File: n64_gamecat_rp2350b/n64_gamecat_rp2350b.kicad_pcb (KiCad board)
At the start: 2 copper layers, 66 x 98 mm, 3 parts, among them U4 RP235x-B

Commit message: V0.6 PCB
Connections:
- U4 pad 1: unconnected-(U4-GPIO0-Pad1) -> CO_AD4
- U4 pad 10: unconnected-(U4-GPIO9-Pad10) -> CO_AD15
- U4 pad 2: unconnected-(U4-GPIO1-Pad2) -> CO_AD11
- U4 pad 3: unconnected-(U4-GPIO2-Pad3) -> CO_AD3
- U4 pad 31: unconnected-(U4-GPIO30-Pad31) -> CO_AD7
- U4 pad 32: READ -> CO_AD8
- U4 pad 33: WRITE -> CO_AD6
- U4 pad 34: ALE_L -> CO_AD9
- U4 pad 35: ALE_H -> CO_AD5
- U4 pad 36: unconnected-(U4-GPIO35-Pad36) -> CO_AD10
- U4 pad 37: unconnected-(U4-GPIO36-Pad37) -> ALE_H
- U4 pad 38: unconnected-(U4-GPIO37-Pad38) -> ALE_L
- U4 pad 39: unconnected-(U4-GPIO38-Pad39) -> WRITE
- U4 pad 4: unconnected-(U4-GPIO3-Pad4) -> CO_AD12
- U4 pad 40: unconnected-(U4-GPIO39-Pad40) -> READ
- U4 pad 41: CO_AD15 -> unconnected-(U4-GPIO40-Pad41)
- U4 pad 42: CO_AD0 -> unconnected-(U4-GPIO41-Pad42)
- U4 pad 43: CO_AD14 -> unconnected-(U4-GPIO42-Pad43)
- U4 pad 44: CO_AD1 -> unconnected-(U4-GPIO43-Pad44)
- U4 pad 45: CO_AD13 -> unconnected-(U4-GPIO44-Pad45)
- U4 pad 46: CO_AD2 -> unconnected-(U4-GPIO45-Pad46)
- U4 pad 47: CO_AD12 -> unconnected-(U4-GPIO46-Pad47)
- U4 pad 48: CO_AD3 -> unconnected-(U4-GPIO47-Pad48)
- U4 pad 49: CO_AD11 -> unconnected-(U4-GPIO48-Pad49)
- U4 pad 5: unconnected-(U4-GPIO4-Pad5) -> CO_AD2
- U4 pad 50: CO_AD4 -> unconnected-(U4-GPIO49-Pad50)
- U4 pad 51: CO_AD10 -> unconnected-(U4-GPIO50-Pad51)
- U4 pad 52: CO_AD5 -> unconnected-(U4-GPIO51-Pad52)
- U4 pad 53: CO_AD9 -> unconnected-(U4-GPIO52-Pad53)
- U4 pad 54: CO_AD6 -> unconnected-(U4-GPIO53-Pad54)
- U4 pad 55: CO_AD8 -> unconnected-(U4-GPIO54-Pad55)
- U4 pad 56: CO_AD7 -> unconnected-(U4-GPIO55-Pad56)
- U4 pad 6: unconnected-(U4-GPIO5-Pad6) -> CO_AD13
- U4 pad 7: unconnected-(U4-GPIO6-Pad7) -> CO_AD1
- U4 pad 8: unconnected-(U4-GPIO7-Pad8) -> CO_AD14
- U4 pad 9: unconnected-(U4-GPIO8-Pad9) -> CO_AD0
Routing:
- net CO_AD15: track 32.4 -> 77.1 mm, vias 0 -> 2
- net CO_AD0: track 33.5 -> 74.8 mm, vias 0 -> 1
- net CO_AD7: track 31.6 -> 71.3 mm, vias 0 -> 2
- net +3V3: track 198.1 -> 161.0 mm
- net CO_AD14: track 32.6 -> 69.7 mm, vias 0 -> 2
- net CO_AD12: track 32.8 -> 68.4 mm, vias 0 -> 2
- net CO_AD1: track 34.1 -> 69.0 mm, vias 0 -> 1
- net CO_AD13: track 33.2 -> 67.3 mm, vias 0 -> 2
- net CO_AD9: track 29.5 -> 62.8 mm, vias 0 -> 1
- net CO_AD6: track 31.0 -> 64.2 mm, vias 0 -> 2
- net CO_AD3: track 34.5 -> 65.8 mm
- net CO_AD2: track 34.5 -> 65.8 mm
- net CO_AD8: track 30.1 -> 60.2 mm, vias 0 -> 1
- net CO_AD11: track 30.3 -> 54.3 mm, vias 0 -> 2
- net CO_AD10: track 31.0 -> 51.3 mm, vias 0 -> 1
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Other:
- board size 66 x 98 mm -> 65 x 89.5 mm
- board text added: "N64 GameCat v0.6 Andrew Thomas (CyanBlob) 10/28/24"
- board text removed: "N64 GameCat v0.5 Andrew Thomas (CyanBlob) 10/17/24"

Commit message: v0.7 PCB; prep for 2350
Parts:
- added J1: C_G_I, Connector_PinHeader_2.54mm:PinHeader_1x03_P2.54mm_Vertical, F.Cu at (164.5, 100.0)
- added J2: TxGRx, Connector_PinHeader_2.54mm:PinHeader_1x03_P2.54mm_Vertical, F.Cu at (103.5, 100.0)
- added J4: 5-+G, Connector_PinSocket_2.54mm:PinSocket_1x04_P2.54mm_Vertical, F.Cu at (164.5, 112.5)
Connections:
- U4 pad 1: CO_AD4 -> TX0
- U4 pad 10: CO_AD15 -> CO_AD14
- U4 pad 11: unconnected-(U4-GPIO10-Pad11) -> CO_AD0
- U4 pad 12: unconnected-(U4-GPIO11-Pad12) -> CO_AD15
- U4 pad 2: CO_AD11 -> RX0
- U4 pad 3: CO_AD3 -> CO_AD4
- U4 pad 4: CO_AD12 -> CO_AD11
- U4 pad 5: CO_AD2 -> CO_AD3
- U4 pad 51: unconnected-(U4-GPIO50-Pad51) -> GND
- U4 pad 53: unconnected-(U4-GPIO52-Pad53) -> 5V
- U4 pad 55: unconnected-(U4-GPIO54-Pad55) -> USB D-
- U4 pad 56: unconnected-(U4-GPIO55-Pad56) -> USB D+
- U4 pad 57: unconnected-(U4-GPIO56-Pad57) -> SWDIO
- U4 pad 58: unconnected-(U4-GPIO57-Pad58) -> SWCLK
- U4 pad 6: CO_AD13 -> CO_AD12
- U4 pad 7: CO_AD1 -> CO_AD2
- U4 pad 8: CO_AD14 -> CO_AD13
- U4 pad 9: CO_AD0 -> CO_AD1
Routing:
- net TX0: track 0.00 -> 91.0 mm
- net RX0: track 0.00 -> 90.3 mm
- net GND: track 368.8 -> 415.1 mm, vias 4 -> 2
- net CO_AD0: track 74.8 -> 108.1 mm, vias 1 -> 2
- net Net-(U2-NC-Pad13): track 78.6 -> 111.7 mm
- net 5V: track 0.00 -> 30.0 mm
- net USB D-: track 0.00 -> 23.3 mm
- net SWDIO: track 0.00 -> 23.2 mm
- net CO_AD15: track 77.1 -> 100.2 mm, vias 2 -> 3
- net USB D+: track 0.00 -> 22.7 mm, vias 0 -> 1
- net SWCLK: track 0.00 -> 22.3 mm
- net CO_AD1: track 69.0 -> 90.7 mm, vias 1 -> 3
- net Net-(U2-NC-Pad39): track 81.1 -> 96.5 mm, vias 0 -> 2
- net WRITE: track 83.5 -> 97.3 mm, vias 0 -> 1
- net +3V3: track 161.0 -> 173.7 mm
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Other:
- board text added: "N64 GameCat v0.7 Andrew Thomas (CyanBlob) 10/28/24"
- board text removed: "N64 GameCat v0.6 Andrew Thomas (CyanBlob) 10/28/24"

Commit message: Add v0.8 PCB
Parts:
- removed J4: 5-+G, Connector_PinSocket_2.54mm:PinSocket_1x04_P2.54mm_Vertical
- added J3: USB, Connector_PinSocket_2.54mm:PinSocket_1x05_P2.54mm_Vertical, F.Cu at (164.5, 111.0)
- J1: value C_G_I -> SWD CGIO
- J2: value TxGRx -> UART TGR
- moved J1 7.00 mm to (164.5, 93.0)
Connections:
- U4 pad 10: CO_AD14 -> CA_AD7
- U4 pad 11: CO_AD0 -> CA_AD8
- U4 pad 12: CO_AD15 -> CA_AD9
- U4 pad 13: unconnected-(U4-GPIO12-Pad13) -> CA_AD10
- U4 pad 14: unconnected-(U4-GPIO13-Pad14) -> CA_AD11
- U4 pad 15: CA_AD7 -> CA_AD12
- U4 pad 16: CA_AD8 -> CA_AD13
- U4 pad 17: CA_AD6 -> CA_AD14
- U4 pad 18: CA_AD9 -> CA_AD15
- U4 pad 19: CA_AD5 -> CO_AD0
- U4 pad 20: CA_AD10 -> CO_AD1
- U4 pad 21: CA_AD4 -> CO_AD2
- U4 pad 22: CA_AD11 -> CO_AD3
- U4 pad 23: CA_AD3 -> CO_AD4
- U4 pad 24: CA_AD12 -> CO_AD5
- U4 pad 25: CA_AD2 -> CO_AD6
- U4 pad 26: CA_AD13 -> CO_AD7
- U4 pad 27: CA_AD1 -> CO_AD8
- U4 pad 28: CA_AD14 -> CO_AD9
- U4 pad 29: CA_AD0 -> CO_AD10
- U4 pad 3: CO_AD4 -> CA_AD0
- U4 pad 30: CA_AD15 -> CO_AD11
- U4 pad 31: CO_AD7 -> CO_AD12
- U4 pad 32: CO_AD8 -> CO_AD13
- U4 pad 33: CO_AD6 -> CO_AD14
- U4 pad 34: CO_AD9 -> CO_AD15
- U4 pad 35: CO_AD5 -> ALE_H
- U4 pad 36: CO_AD10 -> ALE_L
- U4 pad 37: ALE_H -> WRITE
- U4 pad 38: ALE_L -> READ
- U4 pad 39: WRITE -> unconnected-(U4-GPIO38-Pad39)
- U4 pad 4: CO_AD11 -> CA_AD1
- U4 pad 40: READ -> unconnected-(U4-GPIO39-Pad40)
- U4 pad 5: CO_AD3 -> CA_AD2
- U4 pad 6: CO_AD12 -> CA_AD3
- U4 pad 7: CO_AD2 -> CA_AD4
- U4 pad 8: CO_AD13 -> CA_AD5
- U4 pad 9: CO_AD1 -> CA_AD6
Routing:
- net CA_AD0: track 29.1 -> 107.1 mm
- net CA_AD1: track 29.6 -> 101.5 mm
- net CA_AD2: track 30.2 -> 96.0 mm
- net CA_AD3: track 29.8 -> 85.1 mm
- net CO_AD15: track 100.2 -> 51.2 mm, vias 3 -> 1
- net CA_AD4: track 26.7 -> 69.2 mm
- net CO_AD0: track 108.1 -> 66.2 mm, vias 2 -> 1
- net Net-(U2-NC-Pad13): track 111.7 -> 73.2 mm
- net CA_AD15: track 23.8 -> 61.8 mm
- net CA_AD5: track 27.3 -> 58.5 mm
- net RX0: track 90.3 -> 61.9 mm, vias 0 -> 2
- net CO_AD1: track 90.7 -> 62.9 mm, vias 3 -> 1
- net CO_AD14: track 74.0 -> 51.7 mm, vias 4 -> 1
- net TX0: track 91.0 -> 70.3 mm, vias 0 -> 2
- net CA_AD12: track 24.0 -> 44.4 mm
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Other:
- board text added: "N64 GameCat v0.8 Andrew Thomas (CyanBlob) 11/01/24"
- board text removed: "N64 GameCat v0.7 Andrew Thomas (CyanBlob) 10/28/24"

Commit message: Add v0.9 PCB
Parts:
- J1: value SWD CGIO -> Conn_01x03_Pin
- J2: value UART TGR -> Conn_01x03_Pin
- J3: value USB -> Conn_01x05
- moved U4 3.00 mm to (137.0, 102.5)
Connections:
- U4 pad 1: TX0 -> CA_AD0
- U4 pad 10: CA_AD7 -> CA_AD9
- U4 pad 11: CA_AD8 -> CA_AD10
- U4 pad 12: CA_AD9 -> CA_AD11
- U4 pad 13: CA_AD10 -> CA_AD12
- U4 pad 14: CA_AD11 -> CA_AD13
- U4 pad 15: CA_AD12 -> CA_AD14
- U4 pad 16: CA_AD13 -> CA_AD15
- U4 pad 17: CA_AD14 -> unconnected-(U4-GPIO16-Pad17)
- U4 pad 18: CA_AD15 -> unconnected-(U4-GPIO17-Pad18)
- U4 pad 2: RX0 -> CA_AD1
- U4 pad 3: CA_AD0 -> CA_AD2
- U4 pad 35: ALE_H -> unconnected-(U4-GPIO34-Pad35)
- U4 pad 36: ALE_L -> unconnected-(U4-GPIO35-Pad36)
- U4 pad 37: WRITE -> unconnected-(U4-GPIO36-Pad37)
- U4 pad 38: READ -> unconnected-(U4-GPIO37-Pad38)
- U4 pad 4: CA_AD1 -> CA_AD3
- U4 pad 41: unconnected-(U4-GPIO40-Pad41) -> ALE_H
- U4 pad 42: unconnected-(U4-GPIO41-Pad42) -> ALE_L
- U4 pad 43: unconnected-(U4-GPIO42-Pad43) -> WRITE
- U4 pad 44: unconnected-(U4-GPIO43-Pad44) -> READ
- U4 pad 45: unconnected-(U4-GPIO44-Pad45) -> TX0
- U4 pad 46: unconnected-(U4-GPIO45-Pad46) -> RX0
- U4 pad 5: CA_AD2 -> CA_AD4
- U4 pad 6: CA_AD3 -> CA_AD5
- U4 pad 7: CA_AD4 -> CA_AD6
- U4 pad 8: CA_AD5 -> CA_AD7
- U4 pad 9: CA_AD6 -> CA_AD8
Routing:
- net TX0: track 70.3 -> 30.6 mm, vias 2 -> 0
- net RX0: track 61.9 -> 30.1 mm, vias 2 -> 0
- net CA_AD0: track 107.1 -> 78.5 mm, vias 0 -> 1
- net CO_AD10: track 58.2 -> 78.9 mm, vias 2 -> 1
- net CA_AD1: track 101.5 -> 80.9 mm, vias 0 -> 1
- net CO_AD9: track 63.0 -> 83.5 mm, vias 3 -> 2
- net CO_AD3: track 58.4 -> 78.8 mm, vias 2 -> 1
- net CO_AD8: track 60.8 -> 80.5 mm, vias 2 -> 0
- net CO_AD0: track 66.2 -> 85.2 mm
- net CO_AD1: track 62.9 -> 81.9 mm
- net CO_AD2: track 60.6 -> 79.4 mm
- net CA_AD4: track 69.2 -> 51.6 mm, vias 0 -> 1
- net CO_AD11: track 57.9 -> 75.5 mm, vias 2 -> 1
- net ALE_H: track 91.7 -> 108.4 mm
- net ALE_L: track 94.2 -> 79.0 mm, vias 1 -> 2
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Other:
- board size 65 x 89.5 mm -> 65 x 80.5 mm
- board text added: "N64 GameCat v0.9c Andrew Thomas (CyanBlob) 01/16/25"
- board text removed: "N64 GameCat v0.8 Andrew Thomas (CyanBlob) 11/01/24"

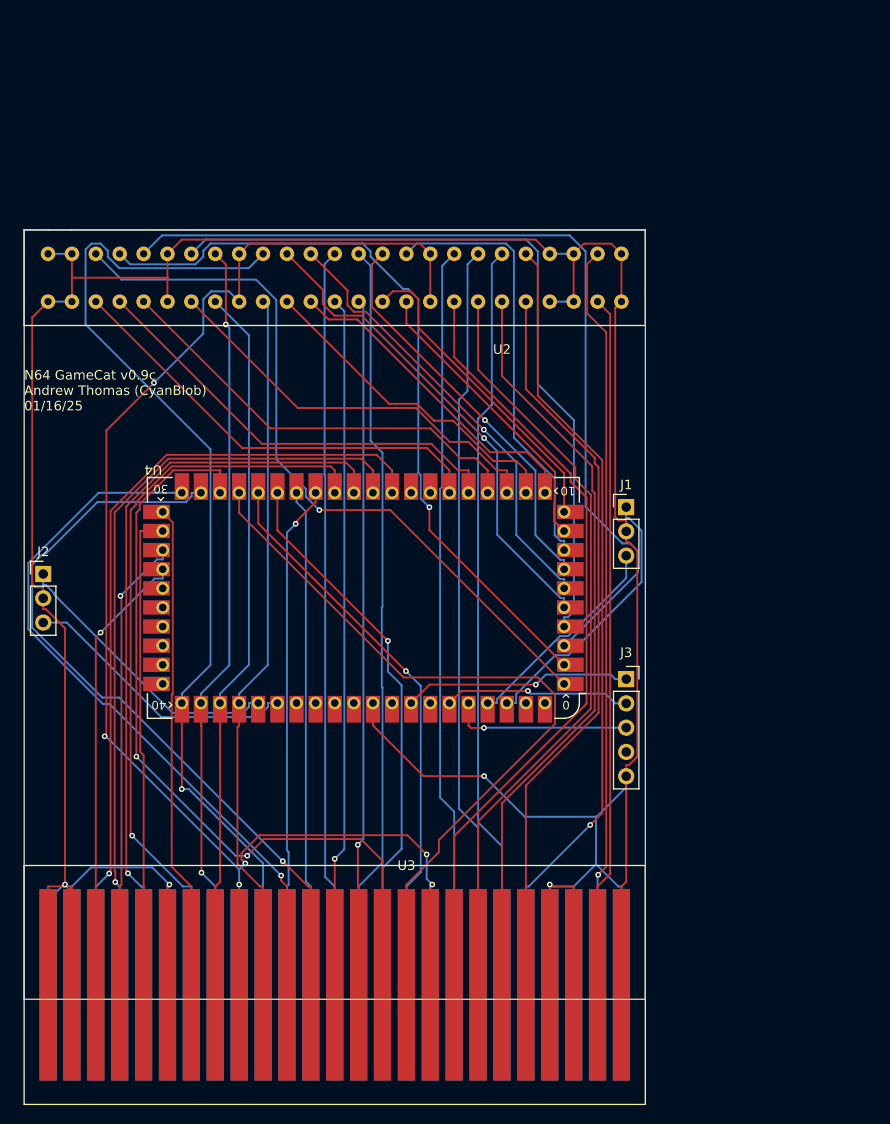
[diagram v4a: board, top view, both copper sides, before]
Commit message: Updates to improve DMA
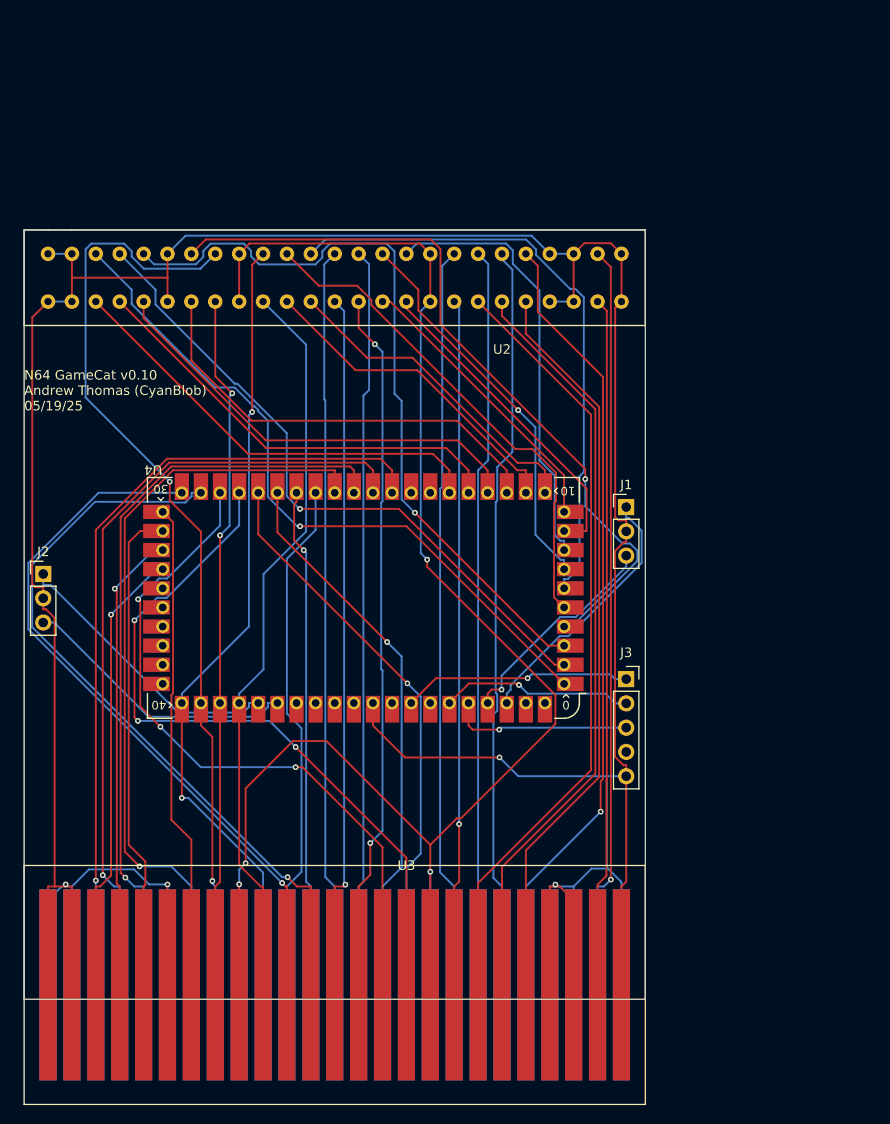
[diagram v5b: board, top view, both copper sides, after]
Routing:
- net ALE_H: track 108.4 -> 83.9 mm, vias 1 -> 2
- net ALE_L: track 79.0 -> 98.5 mm
- net CA_AD5: track 47.6 -> 64.2 mm, vias 1 -> 0
- net CA_AD2: track 95.6 -> 81.1 mm, vias 0 -> 1
- net CA_AD1: track 80.9 -> 69.7 mm
- net Net-(U2-CIC_PIF): track 83.0 -> 71.9 mm, vias 0 -> 1
- net CO_AD9: track 83.5 -> 73.0 mm, vias 2 -> 3
- net +3V3: track 175.6 -> 183.4 mm, vias 6 -> 4
- net CA_AD0: track 78.5 -> 73.9 mm
- net CA_AD12: track 42.7 -> 46.3 mm
- net CO_AD8: track 80.5 -> 77.1 mm, vias 0 -> 3
- net READ: track 74.3 -> 77.4 mm
- net CA_AD9: track 33.8 -> 31.0 mm
- net CA_AD8: track 31.6 -> 34.2 mm
- net Net-(U2-NC-Pad14): track 72.0 -> 73.7 mm, vias 1 -> 2
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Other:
- board text added: "N64 GameCat v0.10 Andrew Thomas (CyanBlob) 05/19/25"
- board text removed: "N64 GameCat v0.9c Andrew Thomas (CyanBlob) 01/16/25"

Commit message: Misc changes; add OoT decomp
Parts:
- removed J1, J2: Conn_01x03_Pin, Connector_PinHeader_2.54mm:PinHeader_1x03_P2.54mm_Vertical
- removed J3: Conn_01x05, Connector_PinSocket_2.54mm:PinSocket_1x05_P2.54mm_Vertical
- added A1: RaspberryPi_Pico, Module:RaspberryPi_Pico_Common_Unspecified, F.Cu at (158.7, 93.6)
- added C1: 10uF, Capacitor_SMD:C_0805_2012Metric, F.Cu at (148.0, 125.0)
- added C2: 100nF, Capacitor_SMD:C_0402_1005Metric, F.Cu at (134.5, 62.5)
- added C3: 100nF, Capacitor_SMD:C_0402_1005Metric, F.Cu at (172.0, 63.0)
- added C4: 100nF, Capacitor_SMD:C_0402_1005Metric, F.Cu at (143.0, 80.0)
- added C5: 100nF, Capacitor_SMD:C_0402_1005Metric, F.Cu at (138.5, 80.5)
- added D1: LED, LED_SMD:LED_0402_1005Metric, F.Cu at (183.0, 79.0)
- added J4: Conn_01x02_Pin, Connector_PinHeader_2.54mm:PinHeader_1x02_P2.54mm_Vertical, F.Cu at (156.5, 67.7)
- added R1: 10K, Resistor_SMD:R_0402_1005Metric, F.Cu at (170.0, 80.0)
- added R2: 10K, Resistor_SMD:R_0402_1005Metric, F.Cu at (145.5, 80.0)
- added R3: 10K, Resistor_SMD:R_0402_1005Metric, F.Cu at (152.0, 112.5)
- added R4: 10K, Resistor_SMD:R_0402_1005Metric, F.Cu at (147.5, 112.5)
- added R5: 1K, Resistor_SMD:R_0402_1005Metric, F.Cu at (180.0, 79.0)
- added SW1: SW_SPDT, Connector_PinSocket_2.54mm:PinSocket_1x03_P2.54mm_Vertical, F.Cu at (161.5, 65.2)
- added U1: ~, n64_library:N64_cartridge_connecter_2.5mm, F.Cu at (160.0, 47.0)
- U2: footprint n64_library:N64_cartridge_connecter_2.5mm -> n64_library:N64_cartridge_pins_2.5mm
- U3: value ~ -> SN74CBTLV3245ADW; footprint n64_library:N64_cartridge_pins_2.5mm -> footprints:DW20
- U4: value RP235x-B -> SN74CBTLV3245ADW; footprint RP2xxx_Stamp:RP2xxx_Stamp_XL_THT -> footprints:DW20
- moved U3 77.2 mm to (180.0, 67.5), turned to 90 degrees
- moved U2 43.1 mm to (152.5, 109.0)
- moved U4 35.4 mm to (142.5, 67.5), turned to 90 degrees
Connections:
- U2 pad 11: CA_AD11 -> AD11
- U2 pad 12: CA_AD10 -> AD10
- U2 pad 13: Net-(U2-NC-Pad13) -> NC
- U2 pad 14: Net-(U2-NC-Pad14) -> NC
- U2 pad 15: CA_AD9 -> AD9
- U2 pad 16: CA_AD8 -> AD8
- U2 pad 17: +3V3 -> 3V3_CART
- U2 pad 18: Net-(U2-CIC_PIF) -> CIC_PIF
- U2 pad 19: Net-(U2-CLK_PIF) -> CLK_PIF
- U2 pad 20: Net-(U2-COLD_RST) -> COLD_RST
- U2 pad 21: Net-(U2-S_DAT) -> S_DAT
- U2 pad 24: Net-(U2-LAUDIO) -> LAUDIO
- U2 pad 28: CA_AD0 -> AD0
- U2 pad 29: CA_AD1 -> AD1
- U2 pad 3: CA_AD15 -> AD15
- U2 pad 30: CA_AD2 -> AD2
- U2 pad 32: CA_AD3 -> AD3
- U2 pad 34: +3V3 -> 3V3_CART
- U2 pad 36: CA_AD4 -> AD4
- U2 pad 37: CA_AD5 -> AD5
- U2 pad 38: Net-(U2-NC-Pad38) -> NC
- U2 pad 39: Net-(U2-NC-Pad39) -> NC
- U2 pad 4: CA_AD14 -> AD14
- U2 pad 40: CA_AD6 -> AD6
- U2 pad 41: CA_AD7 -> AD7
- U2 pad 42: +3V3 -> 3V3_CART
- U2 pad 43: Net-(U2-PIF_CIC) -> PIF_CIC
- U2 pad 44: Net-(U2-JTAG_CLK) -> JTAG_CLK
- U2 pad 45: Net-(U2-NMI_R4300) -> NMI_R4300
- U2 pad 46: Net-(U2-VIDEO_CLK) -> VIDEO_CLK
- U2 pad 49: Net-(U2-R_AUDIO) -> R_AUDIO
- U2 pad 5: CA_AD13 -> AD13
- U2 pad 7: CA_AD12 -> AD12
- U2 pad 9: +3V3 -> 3V3_CART
- U3 pad 1: GND -> NC
- U3 pad 10: READ -> GND
- U3 pad 11: CO_AD11 -> CA_AD7
- U3 pad 12: CO_AD10 -> CA_AD6
- U3 pad 13: Net-(U2-NC-Pad13) -> CA_AD5
- U3 pad 14: Net-(U2-NC-Pad14) -> CA_AD4
- U3 pad 15: CO_AD9 -> CA_AD3
- U3 pad 16: CO_AD8 -> CA_AD2
- U3 pad 17: +3V3 -> CA_AD1
- U3 pad 18: Net-(U2-CIC_PIF) -> CA_AD0
- U3 pad 19: Net-(U2-CLK_PIF) -> CART_EN
- U3 pad 2: GND -> AD0
- U3 pad 20: Net-(U2-COLD_RST) -> 3V3_OUT
- U3 pad 3: CO_AD15 -> AD1
- U3 pad 4: CO_AD14 -> AD2
- U3 pad 5: CO_AD13 -> AD3
- U3 pad 6: GND -> AD4
- U3 pad 7: CO_AD12 -> AD5
- U3 pad 8: WRITE -> AD6
- U3 pad 9: +3V3 -> AD7
- U4 pad 1: CA_AD0 -> NC
- U4 pad 10: CA_AD9 -> GND
- U4 pad 11: CA_AD10 -> CA_AD15
- U4 pad 12: CA_AD11 -> CA_AD14
- U4 pad 13: CA_AD12 -> CA_AD13
- U4 pad 14: CA_AD13 -> CA_AD12
- U4 pad 15: CA_AD14 -> CA_AD11
- U4 pad 16: CA_AD15 -> CA_AD10
- U4 pad 17: unconnected-(U4-GPIO16-Pad17) -> CA_AD9
- U4 pad 18: unconnected-(U4-GPIO17-Pad18) -> CA_AD8
- U4 pad 19: CO_AD0 -> CART_EN
- U4 pad 2: CA_AD1 -> AD8
- U4 pad 20: CO_AD1 -> 3V3_OUT
- U4 pad 3: CA_AD2 -> AD9
- U4 pad 4: CA_AD3 -> AD10
- U4 pad 5: CA_AD4 -> AD11
- U4 pad 6: CA_AD5 -> AD12
- U4 pad 7: CA_AD6 -> AD13
- U4 pad 8: CA_AD7 -> AD14
- U4 pad 9: CA_AD8 -> AD15
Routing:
- net +3V3: track 183.4 -> 0.00 mm, vias 4 -> 0
- net NC: track 0.00 -> 173.7 mm, vias 0 -> 4
- net 3V3_CART: track 0.00 -> 169.5 mm, vias 0 -> 2
- net AD15: track 0.00 -> 136.0 mm, vias 0 -> 3
- net AD4: track 0.00 -> 126.9 mm, vias 0 -> 4
- net AD14: track 0.00 -> 125.4 mm, vias 0 -> 3
- net PIF_CIC: track 0.00 -> 121.8 mm, vias 0 -> 3
- net NMI_R4300: track 0.00 -> 119.0 mm, vias 0 -> 2
- net AD0: track 0.00 -> 117.6 mm, vias 0 -> 3
- net JTAG_CLK: track 0.00 -> 116.4 mm, vias 0 -> 2
- net AD13: track 0.00 -> 115.5 mm, vias 0 -> 1
- net AD11: track 0.00 -> 115.0 mm, vias 0 -> 3
- net AD10: track 0.00 -> 113.8 mm, vias 0 -> 3
- net CLK_PIF: track 0.00 -> 109.9 mm, vias 0 -> 3
- net AD7: track 0.00 -> 107.9 mm, vias 0 -> 6
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- added copper zone on B.Cu, net GND
- added copper zone on F.Cu, net GND
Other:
- board size 65 x 80.5 mm -> 65 x 97 mm
- board text added: "KILL"
- board text added: "PI PICO 2"
- board text added: "USB <-> N64 POWER"
- board text added: "WARNING! NO USB WHILE SWITCH IS UP"
- board text removed: "N64 GameCat v0.10 Andrew Thomas (CyanBlob) 05/19/25"
